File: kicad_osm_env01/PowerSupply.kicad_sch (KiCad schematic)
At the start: 27 parts, among them J5 USB_C_Receptacle_USB2.0, U1 LM66100DCKR, U4 LM66100DCKR, U9 TLV1117LV33DCYR

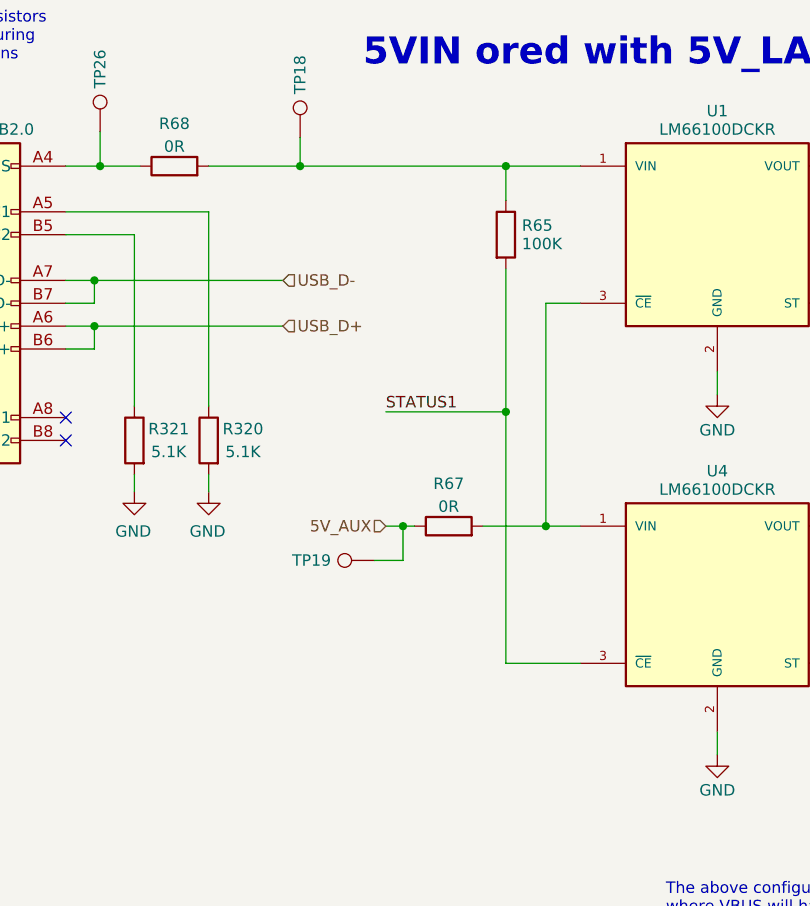
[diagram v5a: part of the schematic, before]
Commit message: updated stm32 pinmap
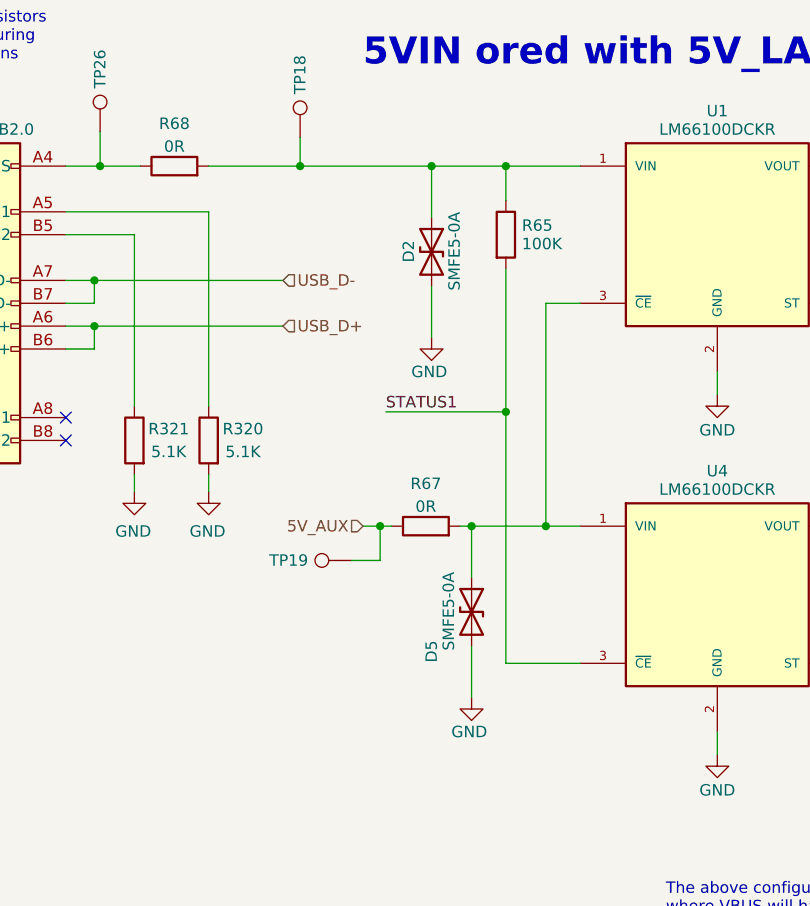
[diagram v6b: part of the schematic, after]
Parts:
- added D2, D5: SMFE5-0A, Diode_SMD:D_SOD-123, symbol Device:D_TVS
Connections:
- net GND: now also D2.2 (A2), D5.2 (A2)
- net at R65.1, R68.2, TP18.1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: now also D2.1 (A1)
- net at R67.2, U1.3 (~{CE}), U4.1 (VIN): now also D5.1 (A1)
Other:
- moved on the sheet: R67, TP19
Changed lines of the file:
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@@
   (junction (at 94.615 35.56) (diameter 0) (color 0 0 0 0)
   )
-  (junction (at 83.185 75.565) (diameter 0) (color 0 0 0 0)
+  (junction (at 80.645 75.565) (diameter 0) (color 0 0 0 0)
   )
   (junction (at 227.965 75.565) (diameter 0) (color 0 0 0 0)
@@
   (junction (at 48.895 53.34) (diameter 0) (color 0 0 0 0)
   )
+  (junction (at 86.36 35.56) (diameter 0) (color 0 0 0 0)
+  )
   (junction (at 196.215 75.565) (diameter 0) (color 0 0 0 0)
   )
@@
   )
   (junction (at 175.895 69.85) (diameter 0) (color 0 0 0 0)
+  )
+  (junction (at 90.805 75.565) (diameter 0) (color 0 0 0 0)
   )
   (junction (at 248.285 90.17) (diameter 0) (color 0 0 0 0)
@@
     (stroke (width 0) (type default))
   )
+  (wire (pts (xy 90.805 94.615) (xy 90.805 88.9))
+    (stroke (width 0) (type default))
+  )
   (wire (pts (xy 26.035 172.085) (xy 26.035 174.625))
     (stroke (width 0) (type default))
@@
     (stroke (width 0) (type default))
   )
-  (wire (pts (xy 83.185 75.565) (xy 84.455 75.565))
+  (wire (pts (xy 80.645 75.565) (xy 81.915 75.565))
     (stroke (width 0) (type default))
   )
@@
     (stroke (width 0) (type default))
   )
-  (wire (pts (xy 92.075 75.565) (xy 99.06 75.565))
+  (wire (pts (xy 89.535 75.565) (xy 90.805 75.565))
     (stroke (width 0) (type default))
   )
@@
     (stroke (width 0) (type default))
   )
+  (wire (pts (xy 86.36 41.275) (xy 86.36 35.56))
+    (stroke (width 0) (type default))
+  )
   (wire (pts (xy 280.035 75.565) (xy 269.875 75.565))
     (stroke (width 0) (type default))
@@
     (stroke (width 0) (type default))
   )
+  (wire (pts (xy 86.36 54.61) (xy 86.36 48.895))
+    (stroke (width 0) (type default))
+  )
   (wire (pts (xy 248.285 78.105) (xy 248.285 75.565))
     (stroke (width 0) (type default))
@@
     (stroke (width 0) (type default))
   )
-  (wire (pts (xy 81.28 75.565) (xy 83.185 75.565))
+  (wire (pts (xy 78.74 75.565) (xy 80.645 75.565))
+    (stroke (width 0) (type default))
+  )
+  (wire (pts (xy 90.805 81.28) (xy 90.805 75.565))
     (stroke (width 0) (type default))
   )
@@
     (stroke (width 0) (type default))
   )
+  (wire (pts (xy 86.36 35.56) (xy 94.615 35.56))
+    (stroke (width 0) (type default))
+  )
   (wire (pts (xy 175.895 75.565) (xy 175.895 69.85))
     (stroke (width 0) (type default))
@@
     (stroke (width 0) (type default))
   )
-  (wire (pts (xy 83.185 75.565) (xy 83.185 79.375))
+  (wire (pts (xy 80.645 75.565) (xy 80.645 79.375))
     (stroke (width 0) (type default))
   )
@@
     (stroke (width 0) (type default))
   )
+  (wire (pts (xy 90.805 75.565) (xy 99.06 75.565))
+    (stroke (width 0) (type default))
+  )
   (wire (pts (xy 137.795 75.565) (xy 137.795 35.56))
     (stroke (width 0) (type default))
@@
     (stroke (width 0) (type default))
   )
-  (wire (pts (xy 71.755 35.56) (xy 94.615 35.56))
+  (wire (pts (xy 71.755 35.56) (xy 86.36 35.56))
     (stroke (width 0) (type default))
   )
@@
     (stroke (width 0) (type default))
   )
-  (wire (pts (xy 80.01 79.375) (xy 83.185 79.375))
+  (wire (pts (xy 77.47 79.375) (xy 80.645 79.375))
     (stroke (width 0) (type default))
   )
@@
     (effects (font (size 1.27 1.27)) (justify left))
   )
-  (hierarchical_label "5V_AUX" (shape input) (at 81.28 75.565 180) (fields_autoplaced)
+  (hierarchical_label "5V_AUX" (shape input) (at 78.74 75.565 180) (fields_autoplaced)
     (effects (font (size 1.27 1.27)) (justify right))
   )
@@
     )
   )
+  (symbol (lib_id "Device:D_TVS") (at 86.36 45.085 270) (unit 1)
+    (in_bom yes) (on_board yes) (dnp no)
+    (property "Reference" "D2" (at 83.82 43.815 0)
+      (effects (font (size 1.27 1.27)) (justify left))
+    )
+    (property "Value" "SMFE5-0A" (at 88.9 40.64 0)
+      (effects (font (size 1.27 1.27)) (justify left))
+    )
+    (property "Footprint" "Diode_SMD:D_SOD-123" (at 86.36 45.085 0)
+      (effects (font (size 1.27 1.27)) hide)
+    )
+    (property "Datasheet" "https://en.wikipedia.org/wiki/Transient-voltage-suppression_diode" (at 86.36 45.085 0)
+      (effects (font (size 1.27 1.27)) hide)
+    )
+    (pin "1")
+    (pin "2")
+    (instances
+      (project "OSM_env01"
+        (path "/ab8b0540-9c9f-4195-88f5-7bed0b0a8ed6/00000000-0000-0000-0000-000060688d25"
+          (reference "D2") (unit 1)
+        )
+      )
+    )
+  )
   (symbol (lib_id "OSM_env01:GND") (at 118.11 60.96 0) (unit 1)
     (in_bom yes) (on_board yes) (dnp no) (fields_autoplaced)
@@
     )
   )
-  (symbol (lib_id "OSM_env01-rescue:Test_Point-Connector-ESP32-EVB_Rev_D-rescue") (at 80.01 79.375 90) (unit 1)
-    (in_bom yes) (on_board yes) (dnp no)
-    (property "Reference" "TP19" (at 73.025 79.375 90)
-      (effects (font (size 1.27 1.27)))
-    )
-    (property "Value" "Test_Point" (at 83.82 78.74 0)
-      (effects (font (size 1.27 1.27)) hide)
-    )
-    (property "Footprint" "TestPoint:TestPoint_Pad_D1.5mm" (at 80.01 74.295 0)
-      (effects (font (size 1.27 1.27)) hide)
-    )
-    (property "Datasheet" "~" (at 80.01 74.295 0)
+  (symbol (lib_id "OSM_env01-rescue:Test_Point-Connector-ESP32-EVB_Rev_D-rescue") (at 77.47 79.375 90) (unit 1)
+    (in_bom yes) (on_board yes) (dnp no)
+    (property "Reference" "TP19" (at 70.485 79.375 90)
+      (effects (font (size 1.27 1.27)))
+    )
+    (property "Value" "Test_Point" (at 81.28 78.74 0)
+      (effects (font (size 1.27 1.27)) hide)
+    )
+    (property "Footprint" "TestPoint:TestPoint_Pad_D1.5mm" (at 77.47 74.295 0)
+      (effects (font (size 1.27 1.27)) hide)
+    )
+    (property "Datasheet" "~" (at 77.47 74.295 0)
       (effects (font (size 1.27 1.27)) hide)
     )
@@
     )
   )
-  (symbol (lib_id "Device:R") (at 88.265 75.565 90) (unit 1)
+  (symbol (lib_id "Device:R") (at 85.725 75.565 90) (unit 1)
     (in_bom yes) (on_board yes) (dnp no) (fields_autoplaced)
-    (property "Reference" "R67" (at 88.265 70.8492 90)
-      (effects (font (size 1.27 1.27)))
-    )
-    (property "Value" "0R" (at 88.265 73.3861 90)
-      (effects (font (size 1.27 1.27)))
-    )
-    (property "Footprint" "Resistor_SMD:R_0805_2012Metric" (at 88.265 77.343 90)
-      (effects (font (size 1.27 1.27)) hide)
-    )
-    (property "Datasheet" "" (at 88.265 75.565 0)
+    (property "Reference" "R67" (at 85.725 70.8492 90)
+      (effects (font (size 1.27 1.27)))
+    )
+    (property "Value" "0R" (at 85.725 73.3861 90)
+      (effects (font (size 1.27 1.27)))
+    )
+    (property "Footprint" "Resistor_SMD:R_0805_2012Metric" (at 85.725 77.343 90)
+      (effects (font (size 1.27 1.27)) hide)
+    )
+    (property "Datasheet" "" (at 85.725 75.565 0)
       (effects (font (size 1.27 1.27)) hide)
     )
@@
     )
   )
+  (symbol (lib_id "Device:D_TVS") (at 90.805 85.09 270) (unit 1)
+    (in_bom yes) (on_board yes) (dnp no)
+    (property "Reference" "D5" (at 86.36 88.265 0)
+      (effects (font (size 1.27 1.27)) (justify left))
+    )
+    (property "Value" "SMFE5-0A" (at 88.265 80.645 0)
+      (effects (font (size 1.27 1.27)) (justify left))
+    )
+    (property "Footprint" "Diode_SMD:D_SOD-123" (at 90.805 85.09 0)
+      (effects (font (size 1.27 1.27)) hide)
+    )
+    (property "Datasheet" "https://en.wikipedia.org/wiki/Transient-voltage-suppression_diode" (at 90.805 85.09 0)
+      (effects (font (size 1.27 1.27)) hide)
+    )
+    (pin "1")
+    (pin "2")
+    (instances
+      (project "OSM_env01"
+        (path "/ab8b0540-9c9f-4195-88f5-7bed0b0a8ed6/00000000-0000-0000-0000-000060688d25"
+          (reference "D5") (unit 1)
+        )
+      )
+    )
+  )
   (symbol (lib_id "power:PWR_FLAG") (at 189.23 65.405 0) (unit 1)
     (in_bom yes) (on_board yes) (dnp no) (fields_autoplaced)
@@
         (path "/ab8b0540-9c9f-4195-88f5-7bed0b0a8ed6/00000000-0000-0000-0000-000060688d25"
           (reference "#FLG03") (unit 1)
+        )
+      )
+    )
+  )
+  (symbol (lib_id "power:GND") (at 86.36 54.61 0) (unit 1)
+    (in_bom yes) (on_board yes) (dnp no)
+    (property "Reference" "#PWR027" (at 86.36 60.96 0)
+      (effects (font (size 1.27 1.27)) hide)
+    )
+    (property "Value" "GND" (at 86.106 58.42 0)
+      (effects (font (size 1.27 1.27)))
+    )
+    (property "Footprint" "" (at 86.36 54.61 0)
+      (effects (font (size 1.524 1.524)))
+    )
+    (property "Datasheet" "" (at 86.36 54.61 0)
+      (effects (font (size 1.524 1.524)))
+    )
+    (pin "1")
+    (instances
+      (project "OSM_env01"
+        (path "/ab8b0540-9c9f-4195-88f5-7bed0b0a8ed6/00000000-0000-0000-0000-000060688d25"
+          (reference "#PWR027") (unit 1)
         )
       )
@@
         )
       )
+    )
+  )
+  (symbol (lib_id "power:GND") (at 90.805 94.615 0) (unit 1)
+    (in_bom yes) (on_board yes) (dnp no)
+    (property "Reference" "#PWR045" (at 90.805 100.965 0)
+      (effects (font (size 1.27 1.27)) hide)
+    )
+    (property "Value" "GND" (at 90.551 98.425 0)
+      (effects (font (size 1.27 1.27)))
+    )
+    (property "Footprint" "" (at 90.805 94.615 0)
+      (effects (font (size 1.524 1.524)))
+    )
+    (property "Datasheet" "" (at 90.805 94.615 0)
+      (effects (font (size 1.524 1.524)))
+    )
+    (pin "1")
+    (instances
+      (project "OSM_env01"
+        (path "/ab8b0540-9c9f-4195-88f5-7bed0b0a8ed6/00000000-0000-0000-0000-000060688d25"
+          (reference "#PWR045") (unit 1)
+        )
+      )

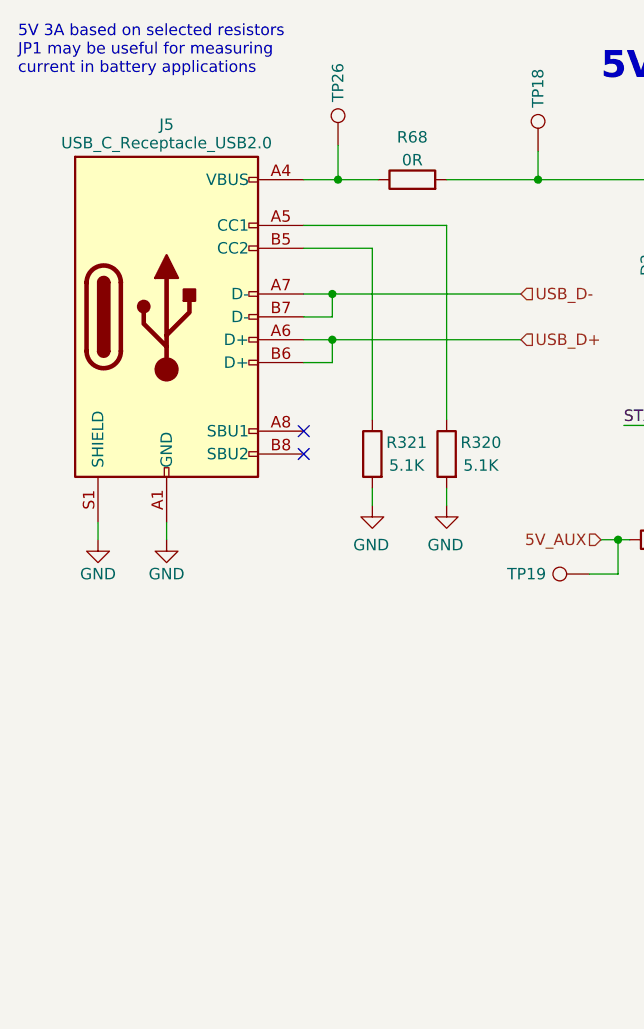
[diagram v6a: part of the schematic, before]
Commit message: updated placement of parts
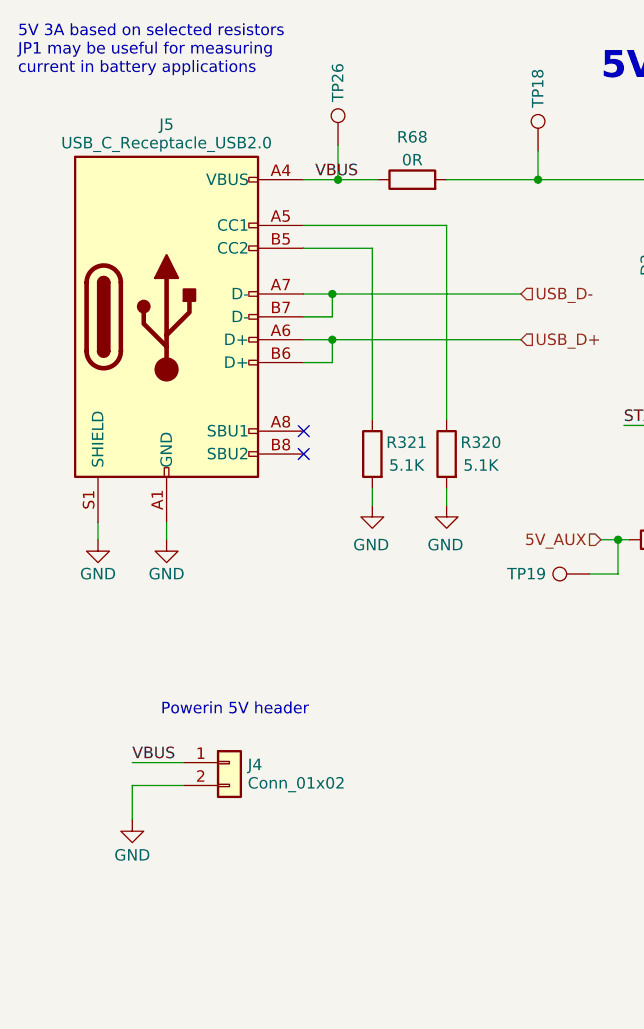
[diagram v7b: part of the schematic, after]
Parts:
- added J4: Conn_01x02, Connector_PinHeader_2.54mm:PinHeader_1x02_P2.54mm_Vertical, symbol Connector_Generic:Conn_01x02
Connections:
- net GND: now also J4.2 (Pin_2)
- net VBUS: now reaches J5.A4 (VBUS), J5.A9 (VBUS), J5.B4 (VBUS), J5.B9 (VBUS), R68.1, TP26.1
- net VBUS: now also J4.1 (Pin_1)
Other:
- note added: "Powerin 5V header"
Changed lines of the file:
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@@
+    (stroke (width 0) (type default))
+  )
+  (wire (pts (xy 32.385 102.87) (xy 26.67 102.87))
     (stroke (width 0) (type default))
   )
@@
     (stroke (width 0) (type default))
   )
+  (wire (pts (xy 26.67 102.87) (xy 26.67 106.68))
+    (stroke (width 0) (type default))
+  )
   (wire (pts (xy 280.035 75.565) (xy 269.875 75.565))
     (stroke (width 0) (type default))
@@
     (stroke (width 0) (type default))
   )
+  (wire (pts (xy 26.67 100.33) (xy 32.385 100.33))
+    (stroke (width 0) (type default))
+  )
   (wire (pts (xy 133.35 75.565) (xy 137.795 75.565))
     (stroke (width 0) (type default))
@@
   (wire (pts (xy 118.11 58.42) (xy 118.11 60.96))
     (stroke (width 0) (type default))
+  )
+  (text "Powerin 5V header" (at 29.845 95.25 0)
+    (effects (font (size 1.27 1.27)) (justify left bottom))
   )
   (text "3V3 Monitor" (at 20.32 141.605 0)
@@
   )
   (label "STATUS1" (at 81.28 62.865 0) (fields_autoplaced)
+    (effects (font (size 1.27 1.27)) (justify left bottom))
+  )
+  (label "VBUS" (at 26.67 100.33 0) (fields_autoplaced)
+    (effects (font (size 1.27 1.27)) (justify left bottom))
+  )
+  (label "VBUS" (at 46.99 35.56 0) (fields_autoplaced)
     (effects (font (size 1.27 1.27)) (justify left bottom))
   )
@@
     )
   )
+  (symbol (lib_id "Connector_Generic:Conn_01x02") (at 37.465 100.33 0) (unit 1)
+    (in_bom yes) (on_board yes) (dnp no) (fields_autoplaced)
+    (property "Reference" "J4" (at 39.497 100.576 0)
+      (effects (font (size 1.27 1.27)) (justify left))
+    )
+    (property "Value" "Conn_01x02" (at 39.497 102.624 0)
+      (effects (font (size 1.27 1.27)) (justify left))
+    )
+    (property "Footprint" "Connector_PinHeader_2.54mm:PinHeader_1x02_P2.54mm_Vertical" (at 37.465 100.33 0)
+      (effects (font (size 1.27 1.27)) hide)
+    )
+    (property "Datasheet" "~" (at 37.465 100.33 0)
+      (effects (font (size 1.27 1.27)) hide)
+    )
+    (pin "1")
+    (pin "2")
+    (instances
+      (project "OSM_env01"
+        (path "/ab8b0540-9c9f-4195-88f5-7bed0b0a8ed6/00000000-0000-0000-0000-000060688d25"
+          (reference "J4") (unit 1)
+        )
+      )
+    )
+  )
   (symbol (lib_id "Device:R") (at 66.04 156.845 0) (unit 1)
     (in_bom yes) (on_board yes) (dnp no)
@@
         )
       )
+    )
+  )
+  (symbol (lib_id "OSM_env01:GND") (at 26.67 106.68 0) (unit 1)
+    (in_bom yes) (on_board yes) (dnp no) (fields_autoplaced)
+    (property "Reference" "#PWR059" (at 26.67 113.03 0)
+      (effects (font (size 1.27 1.27)) hide)
+    )
+    (property "Value" "GND" (at 26.67 110.625 0)
+      (effects (font (size 1.27 1.27)))
+    )
+    (property "Footprint" "" (at 26.67 106.68 0)
+      (effects (font (size 1.524 1.524)))
+    )
+    (property "Datasheet" "" (at 26.67 106.68 0)
+      (effects (font (size 1.524 1.524)))
+    )
+    (pin "1")
+    (instances
+      (project "OSM_env01"
+        (path "/ab8b0540-9c9f-4195-88f5-7bed0b0a8ed6/00000000-0000-0000-0000-000060688d25"
+          (reference "#PWR059") (unit 1)
+        )
+      )

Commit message: Finished schematics and layout
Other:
- note removed: "5V 3A based on selected resistors JP1 may be useful for measuring current in battery applications"
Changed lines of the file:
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@@
     (effects (font (size 2.9972 2.9972) (thickness 0.5994) bold) (justify left bottom))
-  )
-  (text "5V 3A based on selected resistors\nJP1 may be useful for measuring\ncurrent in battery applications\n\n"
-    (at 13.97 26.035 0)
-    (effects (font (size 1.27 1.27)) (justify left bottom))
   )
   (text "divider ratio=47/147=31.97\n5/1024=1adc=4.88mm\n(4.2/4.88m)*0.3197=275.15adc=fully charged and above\n\n"
